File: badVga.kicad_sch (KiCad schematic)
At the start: 37 parts, among them J1 Conn_01x16_Pin, J2 Conn_01x08_Pin, SW1 SW_DIP_x04, U1 27C010, U10 74HC244, U11 CD74HC4040, U12 74LS20, U13 74LS20, U14 74LS30, U15 74LS30, U16 74LS00, U17 CD74HC4040, U18 74LS30, U19 74LS30, U2 74HC245, U20 74LS00, U3 74LS00, U4 74LS32, U5 74HC14, U6 M48Zx2, U7 74HC245, U8 74HC245, U9 74HC245, Y1 TFT660

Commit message: adjust to sbc6309 io
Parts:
- removed J1: Conn_01x16_Pin, symbol Connector:Conn_01x16_Pin
- removed J2: Conn_01x08_Pin, symbol Connector:Conn_01x08_Pin
- removed U10: 74HC244, Package_SO:SOIC-20W_7.5x12.8mm_P1.27mm, symbol 74xx:74HC244
- removed U11, U17: CD74HC4040, Package_SO:SOIC-16_3.9x9.9mm_P1.27mm, symbol 4xxx:4040
- removed unit 2 of U12
- removed unit 1 of U12
- removed unit 1 of U13
- removed unit 1 of U14
- removed unit 1 of U15
- removed unit 3 of U16
- removed unit 4 of U16
- removed unit 1 of U16
- removed unit 2 of U16
- removed unit 1 of U18
- removed unit 1 of U19
- removed unit 3 of U20
- removed unit 1 of U20
- removed unit 4 of U20
- removed unit 2 of U20
- removed unit 2 of U3
- removed unit 1 of U3
- removed unit 3 of U3
- removed U4: 74LS32, Package_SO:SOIC-14_3.9x8.7mm_P1.27mm, symbol 74xx:74LS32
- removed U5: 74HC14, Package_SO:SOIC-14_3.9x8.7mm_P1.27mm, symbol 74xx:74HC14
- removed U6: M48Zx2, Package_DIP:DIP-24_18.0mmx34.29mm_W15.24mm, symbol Memory_RAM:M48Zx2
- removed U7, U9: 74HC245, Package_SO:SOIC-20W_7.5x12.8mm_P1.27mm, symbol 74xx:74HC245
- removed Y1: TFT660, Oscillator:Oscillator_DIP-8, symbol Oscillator:TFT660
- added J1: VGA, Library:CONN_AHDF15A-KG-TAXB_ASM, symbol Connector:DE15_Pins_HighDensity
- added U21: IDT71342, Package_LCC:PLCC-52_THT-Socket, symbol Library:IDT71342
- added U22, U4: GAL16V8, Package_LCC:PLCC-20_THT-Socket, symbol Logic_Programmable:GAL16V8
- added U5: 28C256, symbol Memory_EEPROM:28C256
- added U6: 74LS00, Package_SO:SOIC-14_3.9x8.7mm_P1.27mm, symbol 74xx:74LS00
- C1, C2, C3, C4, C5, C6, C7, C8, C9: LCSC (none) -> C1710
- R3, R4: LCSC (none) -> C25804
- R5: LCSC (none) -> C21190
- U12, U13: LCSC (none) -> C556253
- U14, U15, U18, U19: LCSC (none) -> C547583
- U16, U20, U3: LCSC (none) -> C609793
- U2, U8: LCSC (none) -> C2675537
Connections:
- net ~{RD} is gone; now on net GND: U2.19 (CE), U8.19 (CE)
- net +5V: now also U21.49 (/BSEMR), U21.50 (R/WR), U21.52 (VCC), U22.20 (VCC), U4.20 (VCC), U5.27 (~{WE}), U5.28 (VCC)
- net A0: now also U21.45 (A0R)
- net A1: now also U21.44 (A1R)
- net A10: now also U2.11 (B7), U21.39 (A6R)
- net A2: now also U21.43 (A2R)
- net A3: now also U21.42 (A3R)
- net A4: now also U21.41 (A4R)
- net A5: now also U21.40 (A5R)
- net A6: now also U21.47 (A10R)
- net A7: now also U21.38 (A7R)
- net A8: now also U2.13 (B5), U21.37 (A8R)
- net A9: now also U2.12 (B6), U21.36 (A9R)
- net BLUE: now also J1.3
- net CP438: now also U5.26 (A13)
- net D0: now also U1.12 (A0), U21.27 (I/O0R); no longer U2.2 (A0)
- net D1: now also U1.11 (A1), U21.28 (I/O1R); no longer U2.3 (A1)
- net D2: now also U1.10 (A2), U21.29 (I/O2R); no longer U2.4 (A2)
- net D3: now also U1.9 (A3), U21.30 (I/O3R), U5.10 (A0); no longer U2.5 (A3)
- net D4: now also U1.8 (A4), U21.31 (I/O4R), U5.9 (A1); no longer U2.6 (A4)
- net D5: now also U1.7 (A5), U21.32 (I/O5R), U5.8 (A2); no longer U2.7 (A5)
- net D6: now also U1.6 (A6), U21.33 (I/O6R), U5.7 (A3); no longer U2.8 (A6)
- net D7: now also U1.5 (A7), U21.34 (I/O7R), U5.6 (A4); no longer U2.9 (A7)
- net GND: now also U2.2 (A0), U2.3 (A1), U2.4 (A2), U2.5 (A3), U2.6 (A4), J1.5, J1.6, J1.7, J1.8, U21.1 (/CEL), U21.26 (GND), U21.46 (/OER), U21.48 (A11R), U21.51 (/CER), U22.1 (I1/CLK), U22.10 (GND), U22.11 (I10/~{OE}), U4.1 (I1/CLK), U4.10 (GND), U4.11 (I10/~{OE}), U5.14 (GND), U5.22 (~{OE})
- net GREEN: now also J1.2
- net HB0: now also U4.2 (I2)
- net HB1: now also U4.3 (I3)
- net HB10: now also U5.24 (A9)
- net HB11: now also U5.21 (A10)
- net HB12: now also U5.23 (A11)
- net HB2: now also U4.4 (I4)
- net HSYNC: now also J1.10
- net INV: now also U5.2 (A12)
- net RED: now also J1.1
- net VB1: now also U5.5 (A5)
- net VB2: now also U5.4 (A6)
- net VB3: now also U5.3 (A7)
- net VB4: now also U5.25 (A8)
- net VB7: now also U2.7 (A5)
- net VB8: now also U2.8 (A6)
- net VB9: now also U2.9 (A7)
- net VSYNC: now also J1.13
- net ~{HBlk}: now also U6.12
- net ~{VBlk}: now also U6.13
- net at U2.16 (B2): no longer U1.10 (A2)
- net at U2.17 (B1): no longer U1.11 (A1)
- net at U2.18 (B0): no longer U1.12 (A0)
- net pixel: now reaches R5.1, SW1.1, SW1.2, SW1.3, U1.13 (D0)
- net pixel: now also U4.19 (IO1)
- net at U2.14 (B4): no longer U1.8 (A4)
- net at U2.15 (B3): no longer U1.9 (A3)
- new net: U5.20 (~{CS}), U6.11
- new net AX0: U21.7 (A0L)
- new net AX1: U21.8 (A1L)
- new net AX10: U21.13 (A6L)
- new net AX11: U21.4 (A11L)
- new net AX2: U21.9 (A2L)
- new net AX3: U21.10 (A3L)
- new net AX4: U21.11 (A4L)
- new net AX5: U21.12 (A5L)
- new net AX6: U21.5 (A10L)
- new net AX7: U21.14 (A7L)
- new net AX8: U21.15 (A8L)
- new net AX9: U21.16 (A9L)
- new net A/B: U5.1 (A14)
- new net DC0: U4.5 (I5), U5.11 (D0)
- new net DC1: U4.6 (I6), U5.12 (D1)
- new net DC2: U4.7 (I7), U5.13 (D2)
- new net DC3: U4.8 (I8), U5.15 (D3)
- new net DC4: U4.9 (I9), U5.16 (D4)
- new net DC5: U4.12 (IO8), U5.17 (D5)
- new net DC6: U4.13 (IO7), U5.18 (D6)
- new net DC7: U4.14 (IO6), U5.19 (D7)
- new net DEV0: U22.2 (I2)
- new net DEV1: U22.3 (I3)
- new net DEV2: U22.4 (I4)
- new net DEV3: U22.5 (I5)
- new net DEV4: U22.6 (I6)
- new net DX0: U21.17 (I/O0L)
- new net DX1: U21.18 (I/O1L)
- new net DX2: U21.19 (I/O2L)
- new net DX3: U21.20 (I/O3L)
- new net DX4: U21.21 (I/O4L)
- new net DX5: U21.22 (I/O5L)
- new net DX6: U21.23 (I/O6L)
- new net DX7: U21.24 (I/O7L)
- new net R/~{W}: U22.9 (I9)
- new net R/~{W}X: U21.2 (R/WL)
- new net ~{CS}X: U21.6 (/OEL), U22.19 (IO1)
- new net ~{E}: U22.8 (I8)
- new net ~{OE}X: U21.3 (/BSEML), U22.18 (IO2)
- new net ~{Q}: U22.7 (I7)
- no-connect marks 24 -> 28
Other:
- added sheet interface (interface.kicad_sch)
- added sheet timing (timing.kicad_sch)
- note added: "Address mapping partially redundant in dual port system"
- note added: "VGA output Needs termination resistors"
- moved on the sheet: JP1, R3, R4, R5, SW1, U1, U13B, U3D, U3E, U8

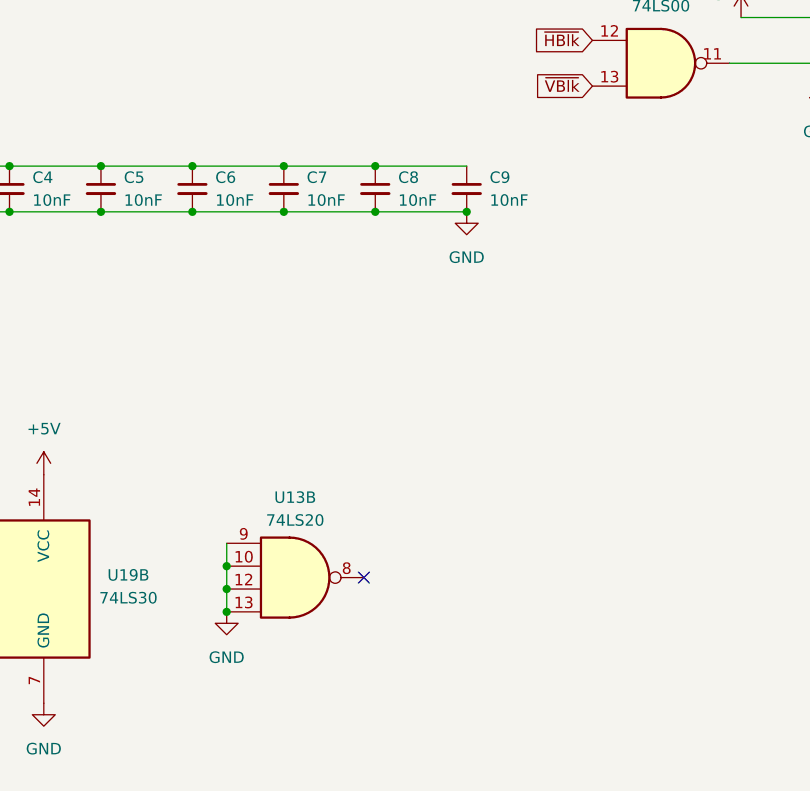
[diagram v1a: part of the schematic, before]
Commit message: fix sync signal generation
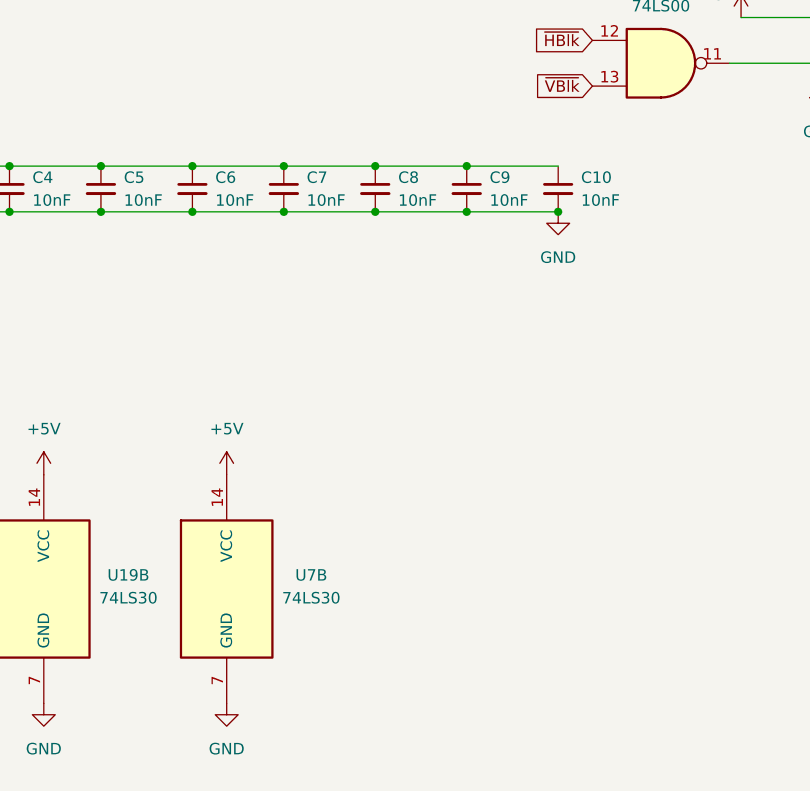
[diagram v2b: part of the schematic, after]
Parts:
- removed unit 2 of U13
- added C10: 10nF, Capacitor_SMD:C_0805_2012Metric, symbol Device:C_Small
- added U7: 74LS30, Package_SO:SOIC-14_3.9x8.7mm_P1.27mm, symbol 74xx:74LS30
- J1: footprint Library:CONN_AHDF15A-KG-TAXB_ASM -> Library:AMPHENOL_ICD15S13E4GX00LF; DigiKey 123-A-HDF15A-KG-TAXB-ND -> 609-5181-ND
- SW1: footprint Package_DIP:DIP-8_W7.62mm -> Button_Switch_THT:SW_DIP_SPSTx04_Slide_6.7x11.72mm_W7.62mm_P2.54mm_LowProfile
- U6: LCSC (none) -> C609793
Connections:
- net +5V: now also C10.1, U7.14 (VCC)
- net GND: now also C10.2, U7.7 (GND)
- no-connect marks 28 -> 27
